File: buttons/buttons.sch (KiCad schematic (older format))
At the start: 25 parts, among them SW1 SW_Push, SW2 SW_Push, SW3 SW_Push, SW4 SW_Push, SW5 SW_Push, U1 74LS04, U2 74LS375, U3 74LS375

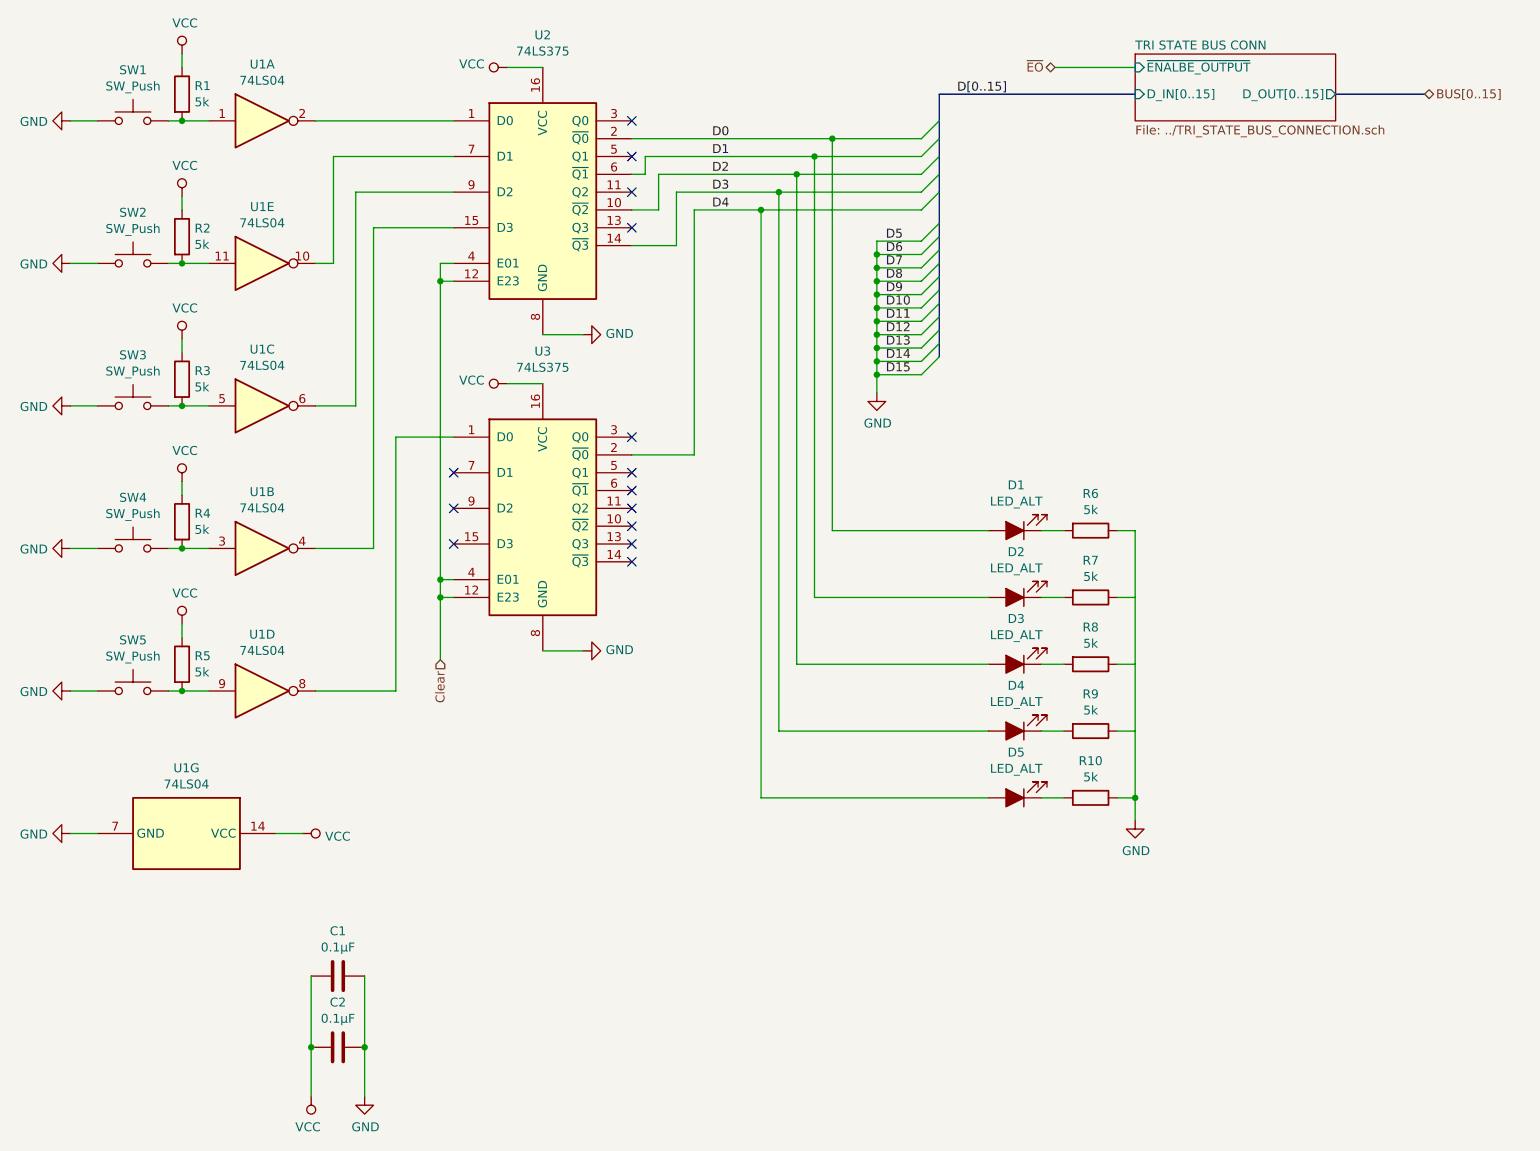
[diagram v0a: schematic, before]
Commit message: add bit operations
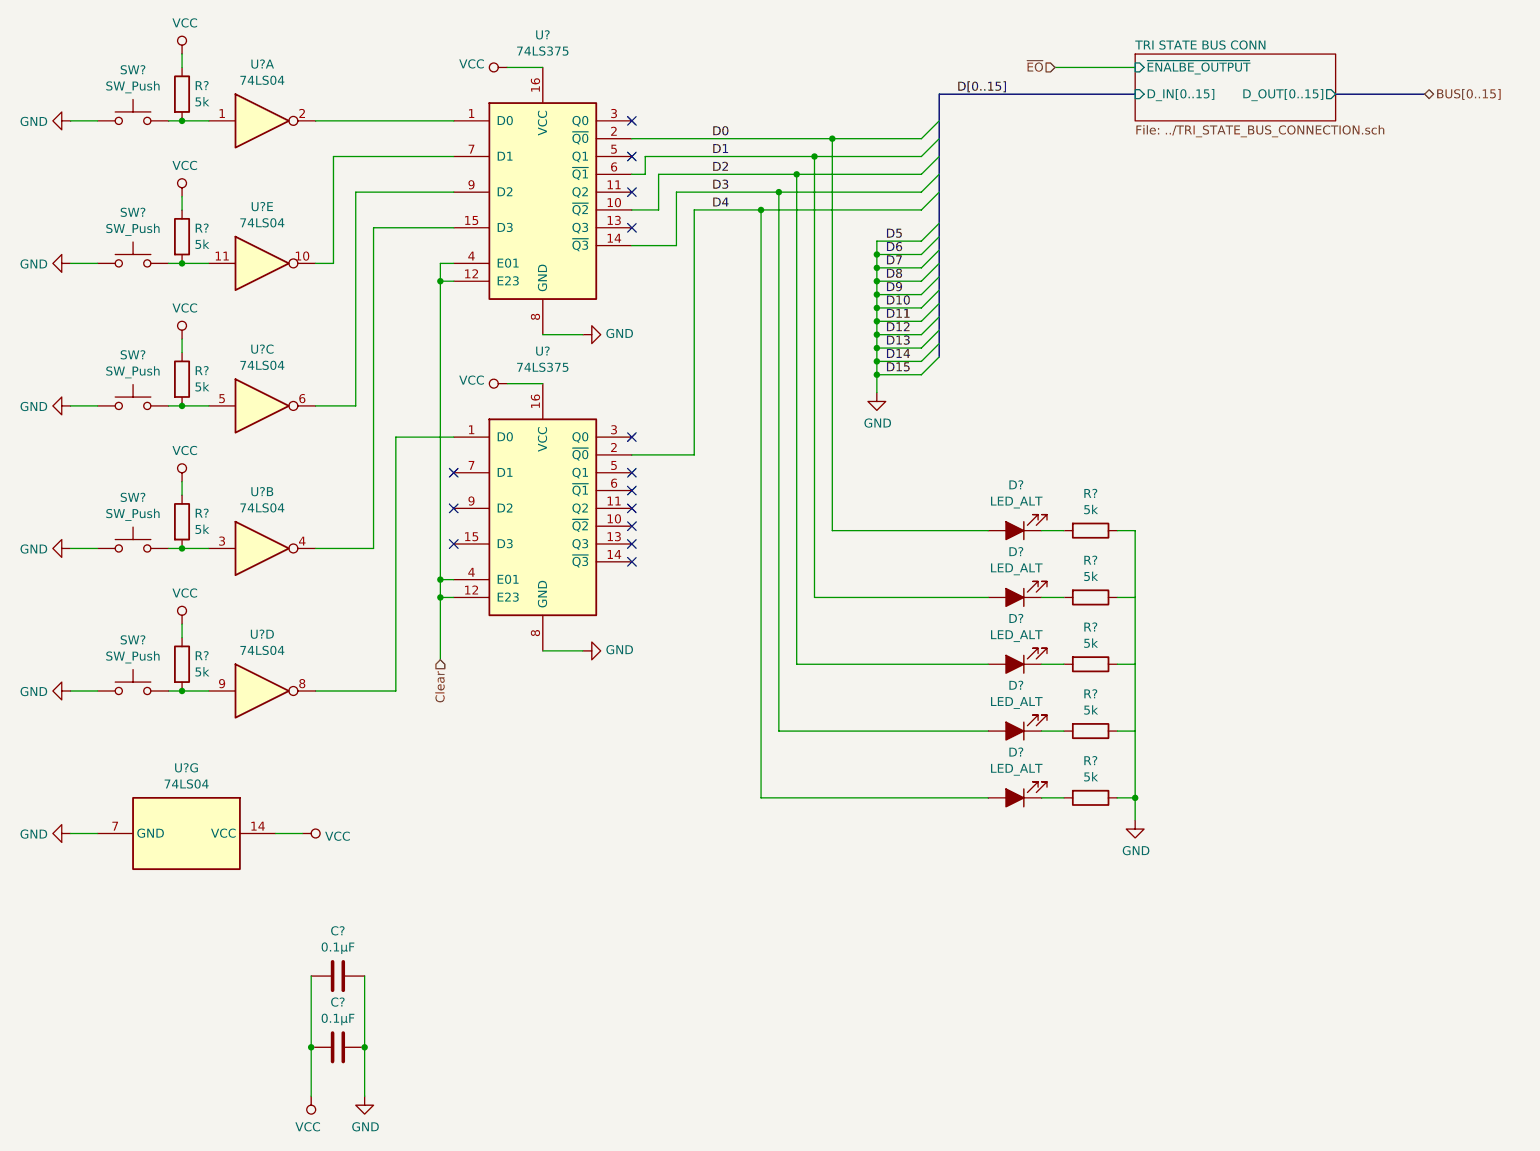
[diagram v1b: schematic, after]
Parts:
- renumbered C1 to C?, C2 to C?, D1 to D?, D2 to D?, D3 to D?, D4 to D?, D5 to D?, R1 to R?, R2 to R?, R3 to R?, R4 to R?, R5 to R?, R6 to R?, R7 to R?, R8 to R?, R9 to R?, R10 to R?, SW1 to SW?, SW2 to SW?, SW3 to SW?, SW4 to SW?, SW5 to SW?, U2 to U?, U3 to U?, U1 to U?

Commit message: part lists
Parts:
- gave numbers to parts that had none: 25
